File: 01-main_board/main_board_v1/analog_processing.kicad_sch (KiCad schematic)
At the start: 29 parts, among them IC6 AD7175-8BCPZ-RL7

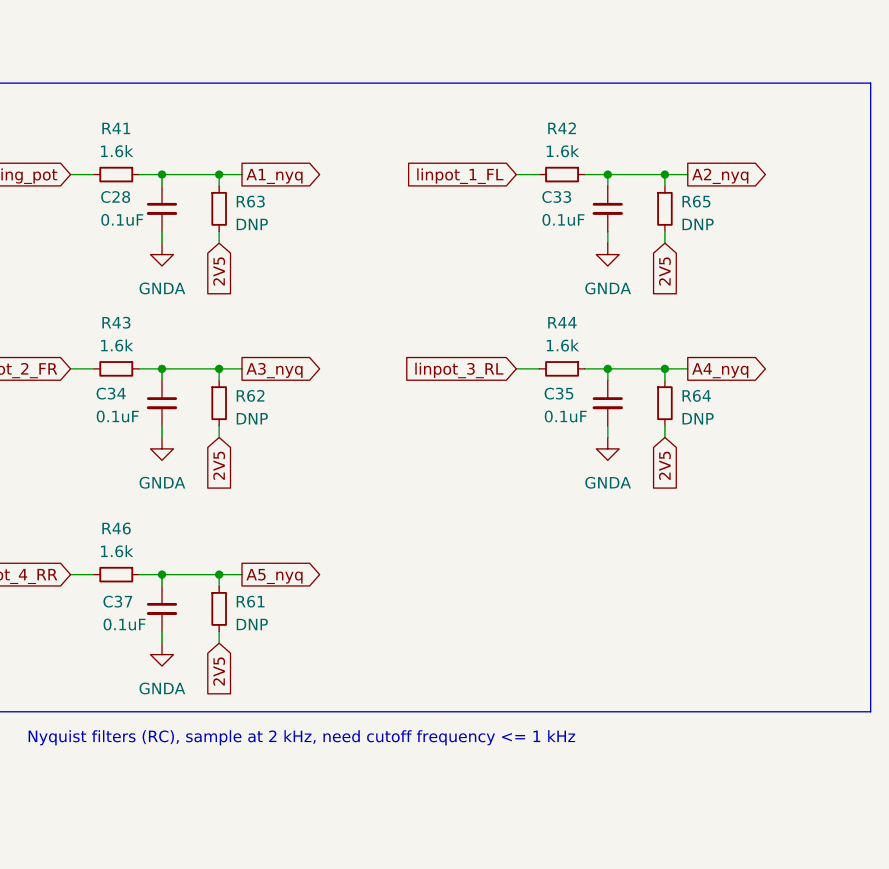
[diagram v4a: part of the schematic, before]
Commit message: matched connector schematic to pinout
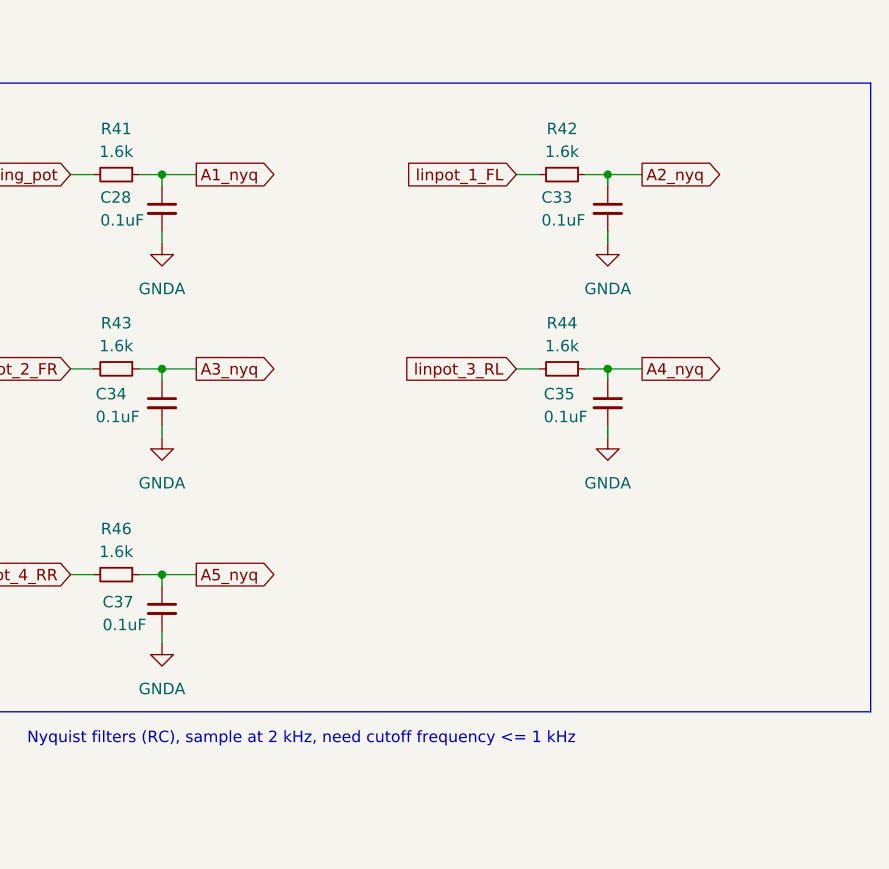
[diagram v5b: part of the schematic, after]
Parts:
- removed R61, R62, R63, R64, R65: DNP, Resistor_SMD:R_0402_1005Metric, symbol Device:R_Small

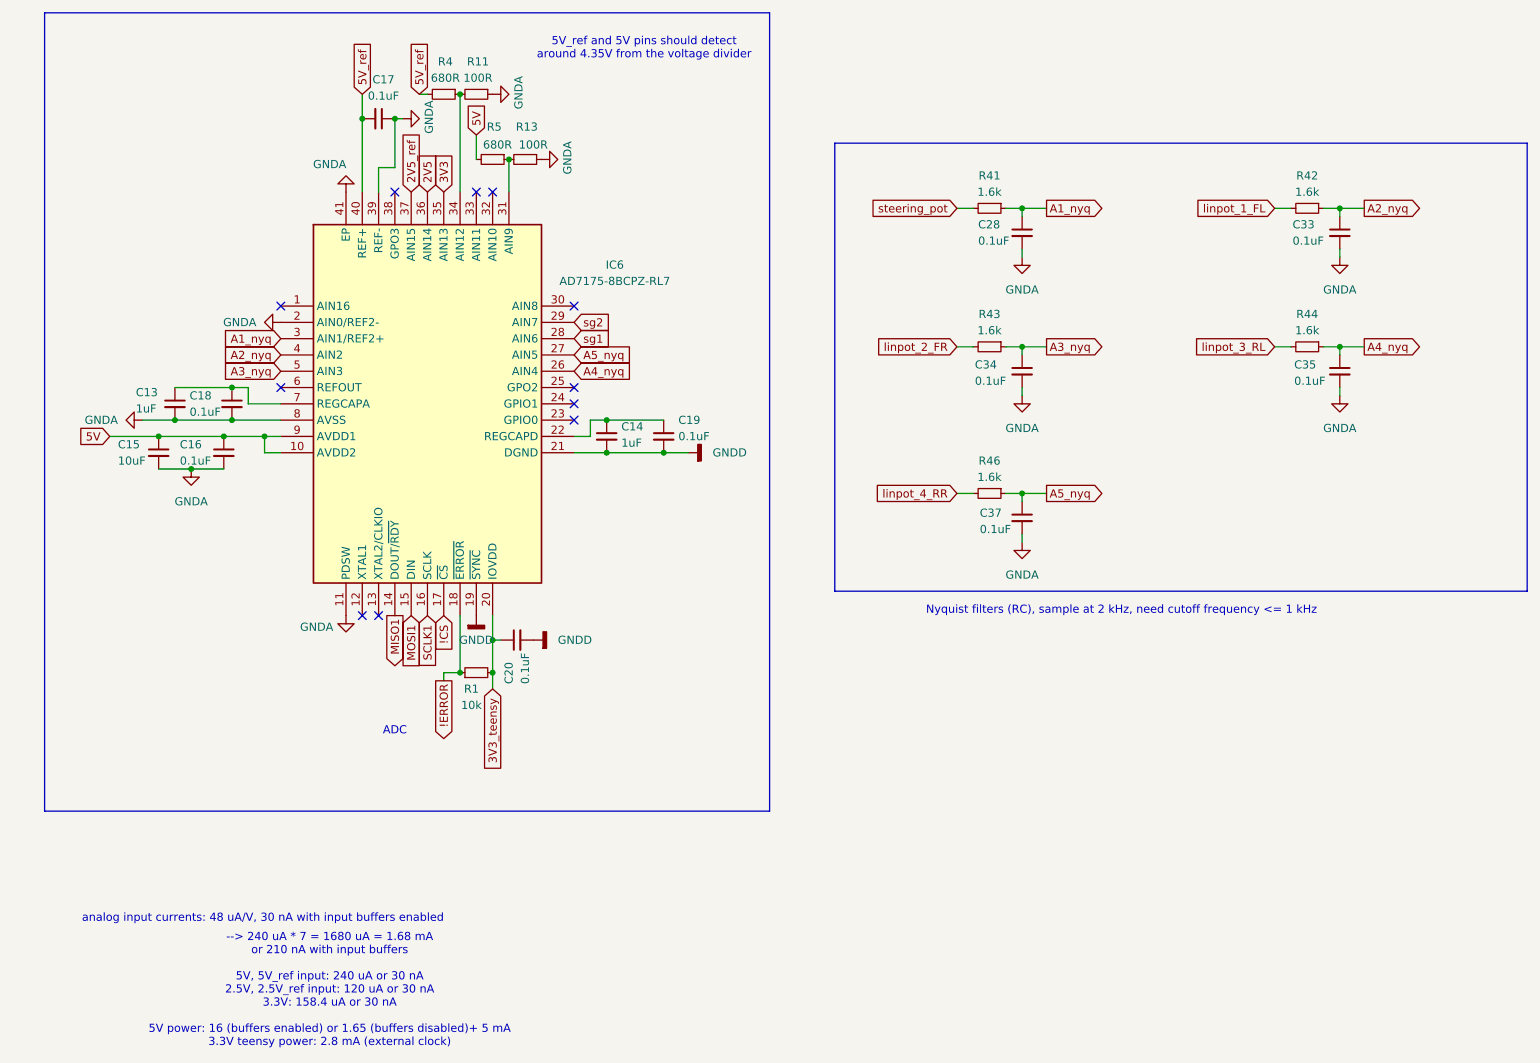
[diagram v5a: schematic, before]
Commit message: grouped externals/ics on layout
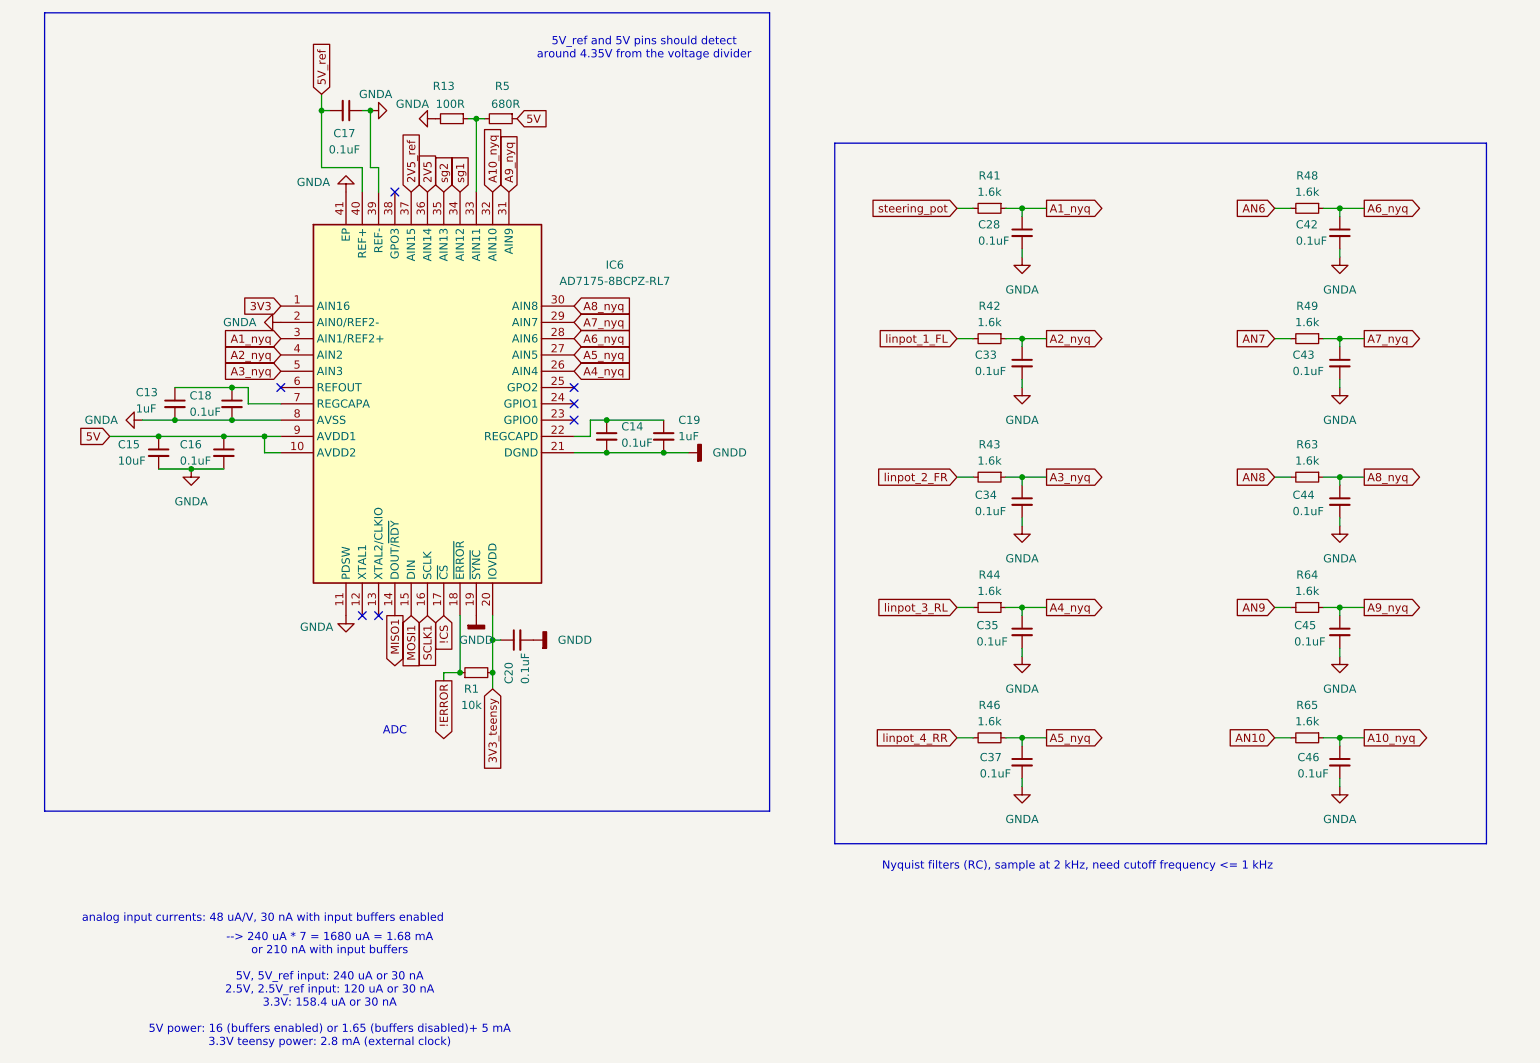
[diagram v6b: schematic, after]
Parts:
- removed R11: 100R, Resistor_SMD:R_0402_1005Metric, symbol Device:R_Small
- removed R4: 680R, Resistor_SMD:R_0402_1005Metric, symbol Device:R_Small
- added C42, C43, C44, C45, C46: 0.1uF, Capacitor_SMD:C_0402_1005Metric, symbol Device:C_Small
- added R48, R49, R63, R64, R65: 1.6k, Resistor_SMD:R_0402_1005Metric, symbol Device:R_Small
- C14: value 1uF -> 0.1uF
- C19: value 0.1uF -> 1uF
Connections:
- net 3V3: now also IC6.1 (AIN16); no longer IC6.35 (AIN13)
- net 5V: now also R5.1; no longer R5.2
- net GNDA: now also R13.2, C42.2, C43.2, C44.2, C45.2, C46.2; no longer R13.1
- net sg1: now also IC6.34 (AIN12); no longer IC6.28 (AIN6)
- net sg2: now also IC6.35 (AIN13); no longer IC6.29 (AIN7)
- net A8_nyq: now reaches IC6.30 (AIN8)
- net A8_nyq: now also C44.1, R63.1
- net A10_nyq: now reaches IC6.32 (AIN10)
- net A10_nyq: now also C46.1, R65.1
- net at IC6.33 (AIN11): now also R13.1, R5.2
- new net A6_nyq: C42.1, IC6.28 (AIN6), R48.1
- new net A7_nyq: C43.1, IC6.29 (AIN7), R49.1
- new net A9_nyq: C45.1, IC6.31 (AIN9), R64.1
- new net AN10: R65.2
- new net AN6: R48.2
- new net AN7: R49.2
- new net AN8: R63.2
- new net AN9: R64.2
- no-connect marks 11 -> 7
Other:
- moved on the sheet: C17, C33, C34, C35, C37, R13, R42, R43, R44, R46, R5

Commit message: finished analog input traces
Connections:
- net linpot_1_FL: now also R41.2; no longer R42.2
- net linpot_2_FR: now also R42.2; no longer R43.2
- net linpot_3_RL: now also R43.2; no longer R44.2
- net linpot_4_RR: now also R44.2; no longer R46.2
- net steering_pot: now also R46.2; no longer R41.2

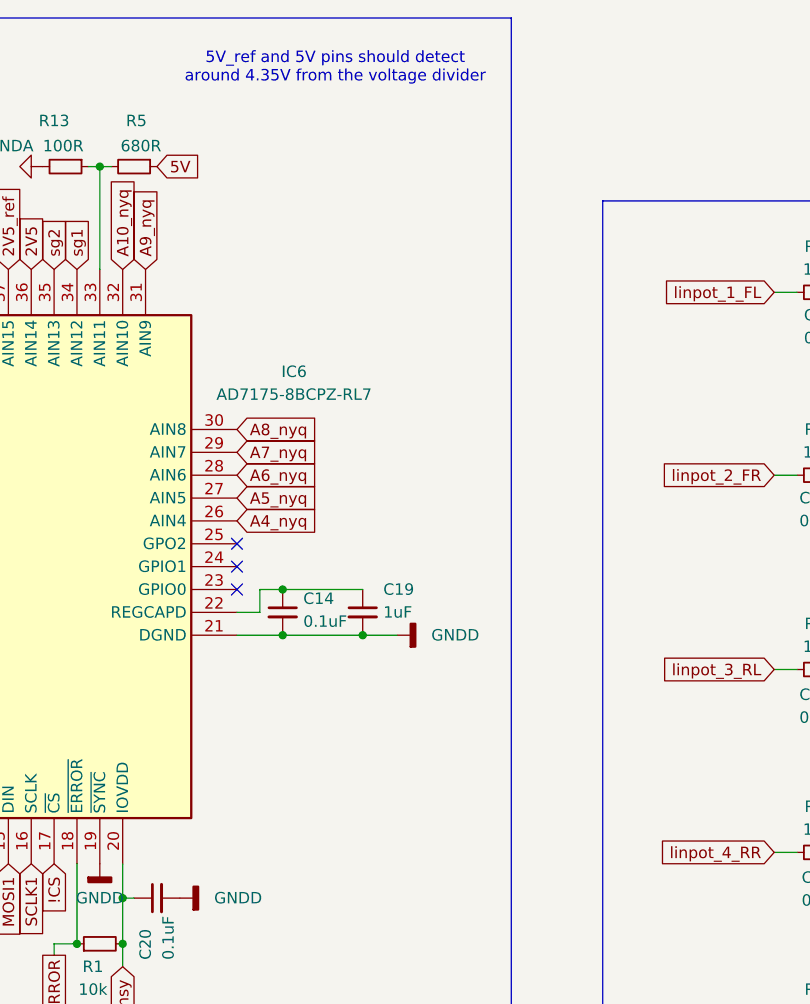
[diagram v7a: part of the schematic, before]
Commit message: added spi and 5V test flags
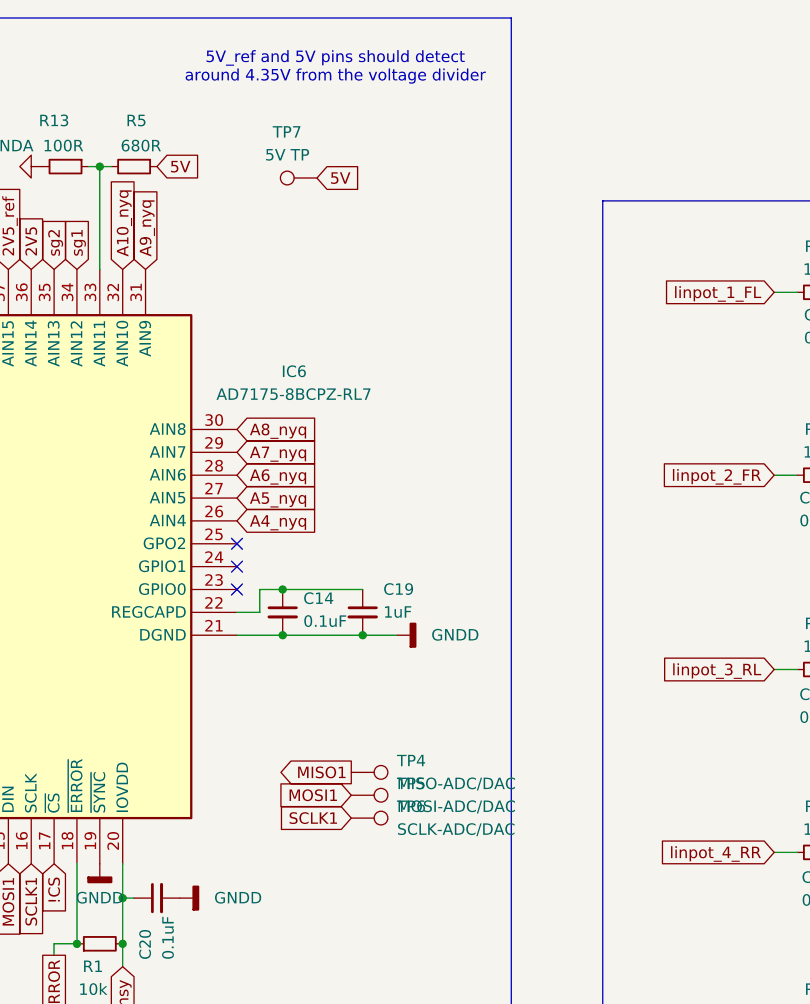
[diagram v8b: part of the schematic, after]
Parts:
- added TP4: MISO-ADC/DAC, TestPoint:TestPoint_Pad_1.0x1.0mm, symbol Connector:TestPoint
- added TP5: MOSI-ADC/DAC, TestPoint:TestPoint_Pad_1.0x1.0mm, symbol Connector:TestPoint
- added TP6: SCLK-ADC/DAC, TestPoint:TestPoint_Pad_1.0x1.0mm, symbol Connector:TestPoint
- added TP7: 5V TP, TestPoint:TestPoint_Pad_1.0x1.0mm, symbol Connector:TestPoint
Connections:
- net 5V: now also TP7.1
- net MISO1: now also TP4.1
- net MOSI1: now also TP5.1
- net SCLK1: now also TP6.1
